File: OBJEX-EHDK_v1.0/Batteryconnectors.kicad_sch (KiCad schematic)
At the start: 15 parts, among them J1 Conn_LiPoBattery, J2 JST_SM02B, J3 Conn_01x03, Q1 NTNUS3171PZT5G

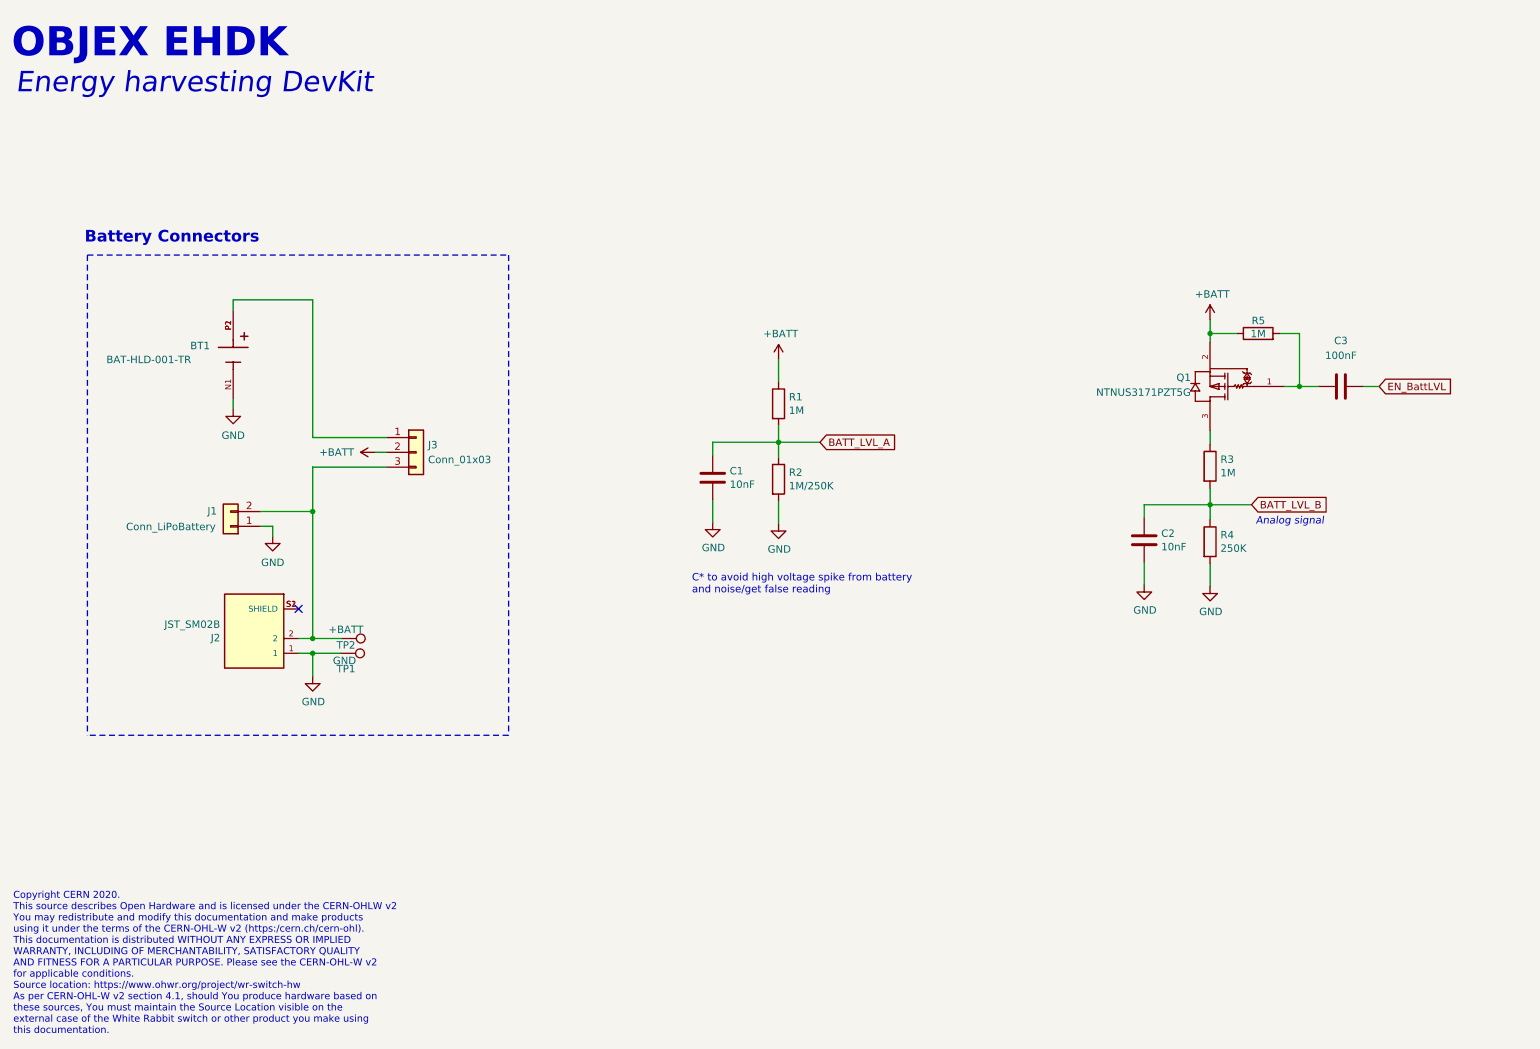
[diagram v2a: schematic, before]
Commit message: Update design, EH ICs & Battery conn
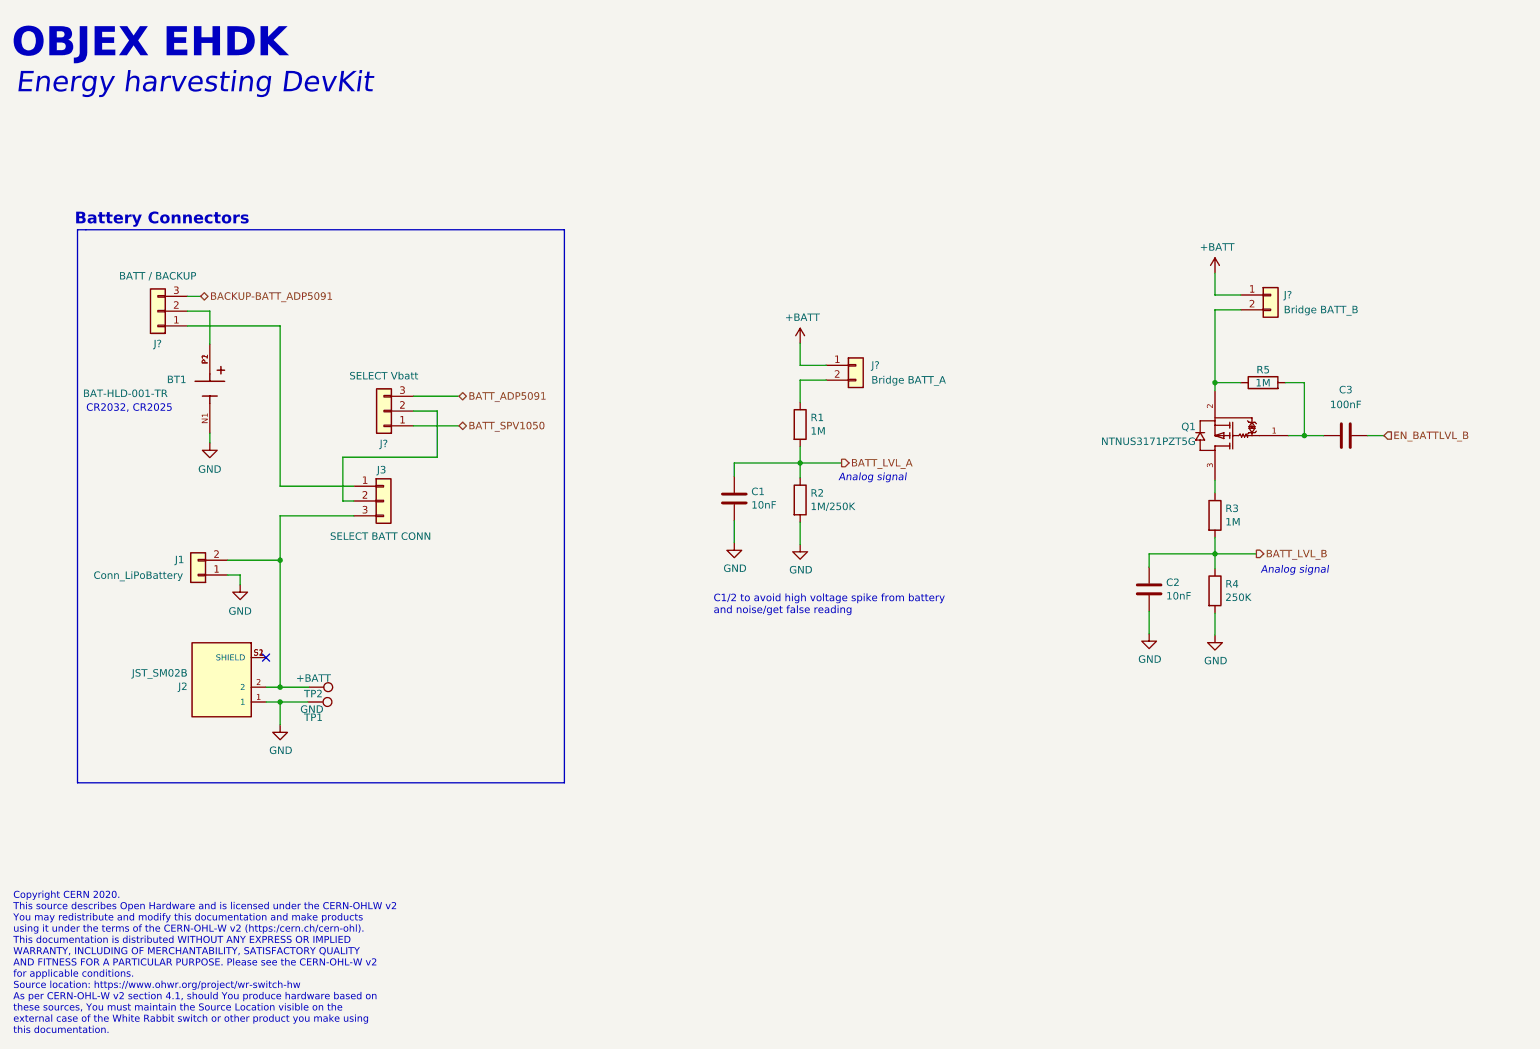
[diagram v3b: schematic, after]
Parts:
- added J?: Bridge BATT_B, symbol Connector_Generic:Conn_01x02
- added J?: Bridge BATT_A, symbol Connector_Generic:Conn_01x02
- added J?: SELECT Vbatt, symbol Connector_Generic:Conn_01x03
- added J?: BATT / BACKUP, symbol Connector_Generic:Conn_01x03
- J3: value Conn_01x03 -> SELECT BATT CONN
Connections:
- net +BATT: now also J?.1 (Pin_1), J?.1 (Pin_1); no longer J3.2 (Pin_2), Q1.2, R1.1, R5.1
- net at BT1.P1, BT1.P2: now also J?.2 (Pin_2); no longer J3.1 (Pin_1)
- net EN_BattLVL renamed EN_BATTLVL_B
- new net: J?.2 (Pin_2), Q1.2, R5.1
- new net: J?.2 (Pin_2), R1.1
- new net: J3.2 (Pin_2), J?.2 (Pin_2)
- new net: J3.1 (Pin_1), J?.1 (Pin_1)
- new net BACKUP-BATT_ADP5091: J?.3 (Pin_3)
- new net BATT_ADP5091: J?.3 (Pin_3)
- new net BATT_SPV1050: J?.1 (Pin_1)
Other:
- note added: "C1/2 to avoid high voltage spike from battery and noise/get false reading"
- note added: "CR2032, CR2025"
- note removed: "C* to avoid high voltage spike from battery and noise/get false reading"
- moved on the sheet: BT1, C1, C2, C3, J1, J2, J3, Q1, R1, R2, R3, R4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

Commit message: update
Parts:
- removed J3: SELECT BATT CONN, symbol Connector_Generic:Conn_01x03
- removed J?: SELECT Vbatt, symbol Connector_Generic:Conn_01x03
- removed TP1: GND, TestPoint:TestPoint_Pad_1.5x1.5mm, symbol Connector:TestPoint
- removed TP2: +BATT, TestPoint:TestPoint_Pad_1.5x1.5mm, symbol Connector:TestPoint
- added J?: Conn_LiPoBattery, symbol Connector_Generic:Conn_01x02
- added J?: JST_SM02B, KicadLibrary:JST_SM02B-SURS-TF(LF)(SN), symbol SM02B-SURS-TF_LF__SN_:SM02B-SURS-TF(LF)(SN)
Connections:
- net BATT_ADP5091: now also J?.2, J?.2 (Pin_2)
- net BATT_SPV1050: now also J1.2 (Pin_2), J2.2, J?.1 (Pin_1)
- net GND: now also J?.1, J?.1 (Pin_1)
- new net: J?.S1 (SHIELD), J?.S2 (SHIELD)
- no-connect marks 1 -> 2
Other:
- moved on the sheet: BT1, C1, C2, C3, J1, J2, J?, Q1, R1, R2, R3, R4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

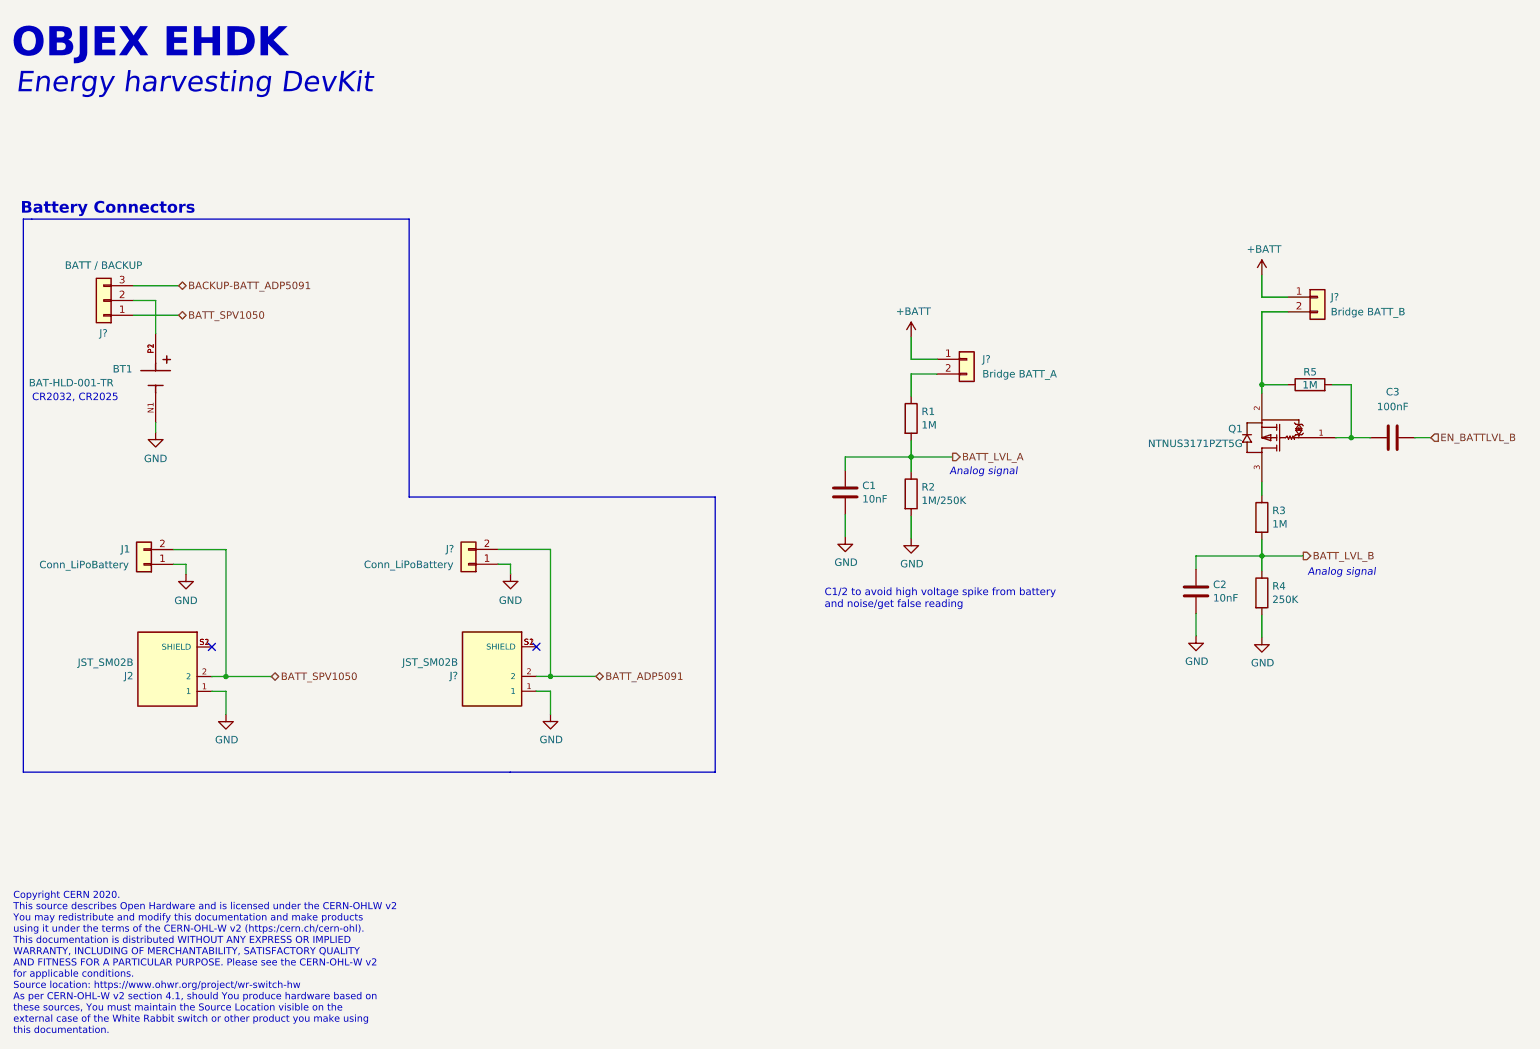
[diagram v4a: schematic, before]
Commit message: Fix, add test points
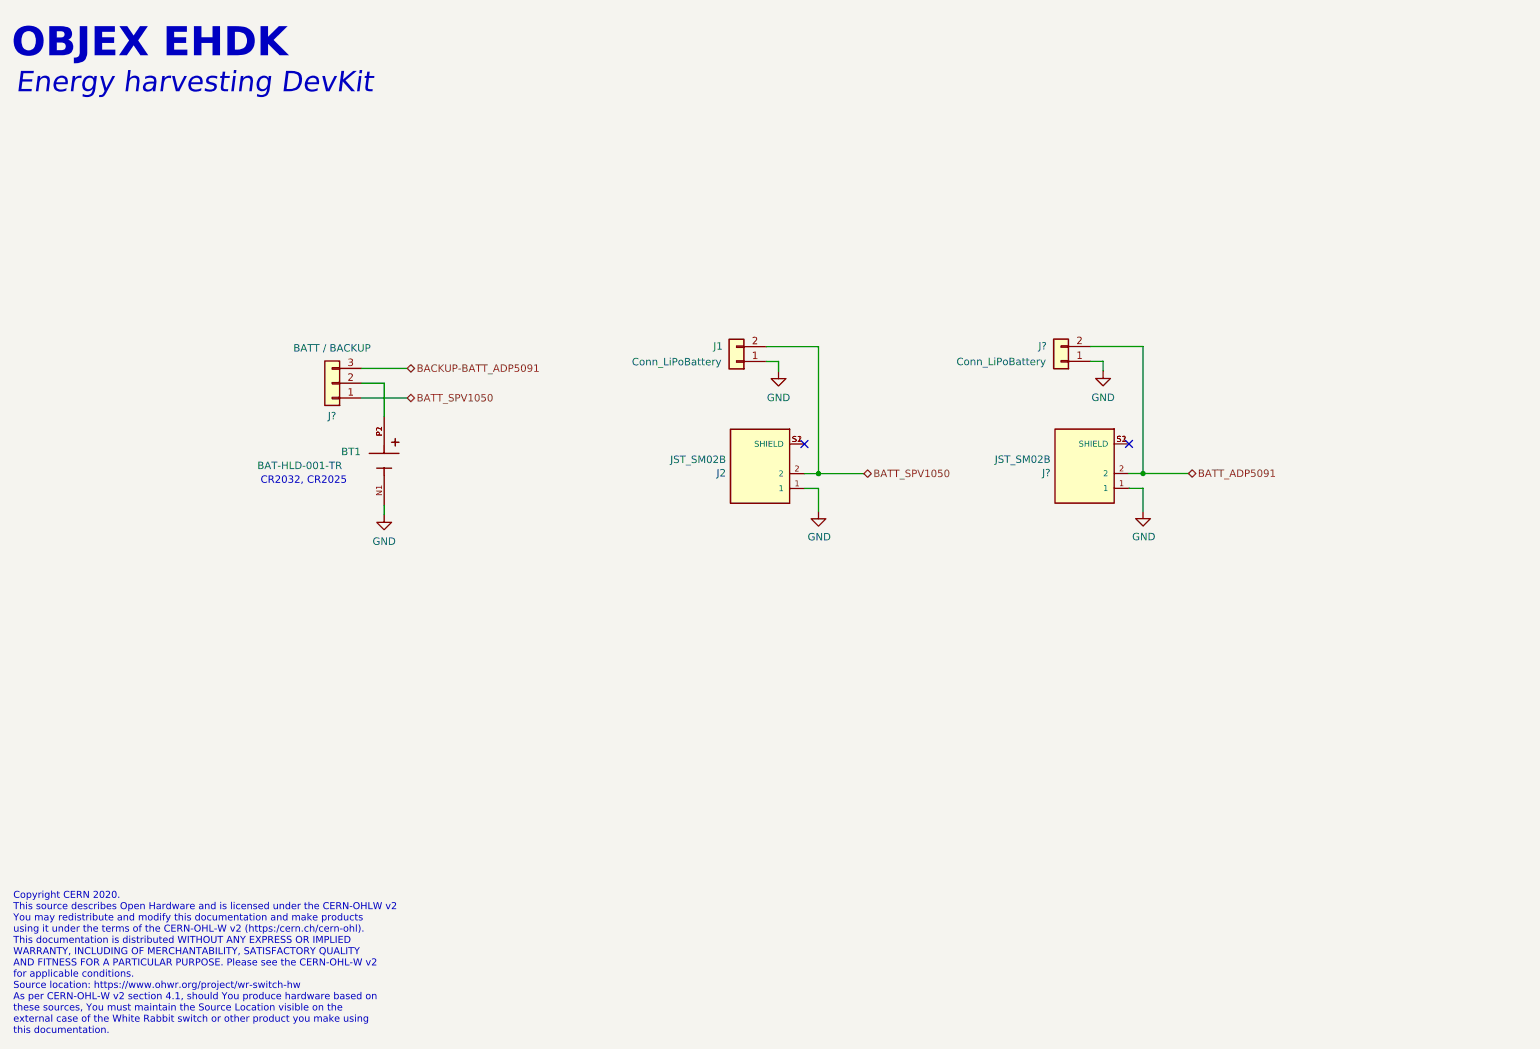
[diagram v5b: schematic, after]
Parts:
- removed C1, C2: 10nF, Capacitor_SMD:C_0402_1005Metric, symbol Device:C
- removed C3: 100nF, Capacitor_SMD:C_0402_1005Metric, symbol Device:C
- removed J?: Bridge BATT_B, symbol Connector_Generic:Conn_01x02
- removed J?: Bridge BATT_A, symbol Connector_Generic:Conn_01x02
- removed Q1: NTNUS3171PZT5G, lib:ONSC-SOT-1123-3-524AA_V, symbol NTNUS3171PZT5G:NTNUS3171PZT5G
- removed R1, R3, R5: 1M, Resistor_SMD:R_0402_1005Metric, symbol Device:R
- removed R2: 1M/250K, Resistor_SMD:R_0402_1005Metric, symbol Device:R
- removed R4: 250K, Resistor_SMD:R_0402_1005Metric, symbol Device:R
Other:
- note removed: "Analog signal"
- note removed: "Battery Connectors"
- note removed: "C1/2 to avoid high voltage spike from battery and noise/get false reading"
- moved on the sheet: BT1, J1, J2, J?

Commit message: SCH Ready for first review
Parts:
- BT1: footprint BAT_BAT-HLD-001-TR -> lib:BAT_BAT-HLD-001-TR
- J1: footprint (none) -> Connector_PinHeader_2.54mm:PinHeader_1x02_P2.54mm_Vertical
- J3: renamed from J?; footprint (none) -> Connector_PinHeader_2.54mm:PinHeader_1x03_P2.54mm_Vertical
- J4: renamed from J?; footprint (none) -> Connector_PinHeader_2.54mm:PinHeader_1x02_P2.54mm_Vertical
- gave numbers to parts that had none: 1
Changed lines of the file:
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@@
   (symbol (lib_id "Connector_Generic:Conn_01x02") (at 198.8312 78.232 180) (unit 1)
     (in_bom yes) (on_board yes)
-    (property "Reference" "J?" (id 0) (at 195.6562 75.6158 0))
+    (property "Reference" "J4" (id 0) (at 195.6562 75.6158 0))
     (property "Value" "Conn_LiPoBattery" (id 1) (at 188.5696 78.3082 0))
-    (property "Footprint" "" (id 2) (at 198.8312 78.232 0)
+    (property "Footprint" "Connector_PinHeader_2.54mm:PinHeader_1x02_P2.54mm_Vertical" (id 2) (at 198.8312 78.232 0)
       (effects (font (size 1.27 1.27)) hide)
     )
@@
     (property "Reference" "J1" (id 0) (at 139.954 75.6412 0))
     (property "Value" "Conn_LiPoBattery" (id 1) (at 132.8674 78.3336 0))
-    (property "Footprint" "" (id 2) (at 143.129 78.2574 0)
+    (property "Footprint" "Connector_PinHeader_2.54mm:PinHeader_1x02_P2.54mm_Vertical" (id 2) (at 143.129 78.2574 0)
       (effects (font (size 1.27 1.27)) hide)
     )
@@
   (symbol (lib_id "SM02B-SURS-TF_LF__SN_:SM02B-SURS-TF(LF)(SN)") (at 202.8698 97.4852 180) (unit 1)
     (in_bom yes) (on_board yes)
-    (property "Reference" "J?" (id 0) (at 197.0278 97.3836 0)
+    (property "Reference" "J5" (id 0) (at 197.0278 97.3836 0)
       (effects (font (size 1.27 1.27)) (justify left))
     )
@@
       (effects (font (size 1.27 1.27)) (justify left))
     )
-    (property "Footprint" "BAT_BAT-HLD-001-TR" (id 2) (at 82.6516 95.3008 0)
+    (property "Footprint" "lib:BAT_BAT-HLD-001-TR" (id 2) (at 82.6516 95.3008 0)
       (effects (font (size 1.27 1.27)) (justify left bottom) hide)
     )
@@
   (symbol (lib_id "Connector_Generic:Conn_01x03") (at 73.7362 81.9912 180) (unit 1)
     (in_bom yes) (on_board yes)
-    (property "Reference" "J?" (id 0) (at 73.7108 87.6046 0))
+    (property "Reference" "J3" (id 0) (at 73.7108 87.6046 0))
     (property "Value" "BATT / BACKUP" (id 1) (at 73.7108 75.9714 0))
-    (property "Footprint" "" (id 2) (at 73.7362 81.9912 0)
+    (property "Footprint" "Connector_PinHeader_2.54mm:PinHeader_1x03_P2.54mm_Vertical" (id 2) (at 73.7362 81.9912 0)
       (effects (font (size 1.27 1.27)) hide)
     )
@@
   (symbol (lib_id "power:GND") (at 212.9028 103.9622 0) (unit 1)
     (in_bom yes) (on_board yes)
-    (property "Reference" "#PWR?" (id 0) (at 212.9028 110.3122 0)
+    (property "Reference" "#PWR0104" (id 0) (at 212.9028 110.3122 0)
       (effects (font (size 1.27 1.27)) hide)
     )
@@
   (symbol (lib_id "power:GND") (at 206.0448 79.9084 0) (unit 1)
     (in_bom yes) (on_board yes) (fields_autoplaced)
-    (property "Reference" "#PWR?" (id 0) (at 206.0448 86.2584 0)
+    (property "Reference" "#PWR0101" (id 0) (at 206.0448 86.2584 0)
       (effects (font (size 1.27 1.27)) hide)
     )
